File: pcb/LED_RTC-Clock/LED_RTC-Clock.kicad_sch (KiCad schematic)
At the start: 5 parts, among them J1 Jack_DC_5V, J2 LED_Matrix, J3 LED_DC, J4 RTC

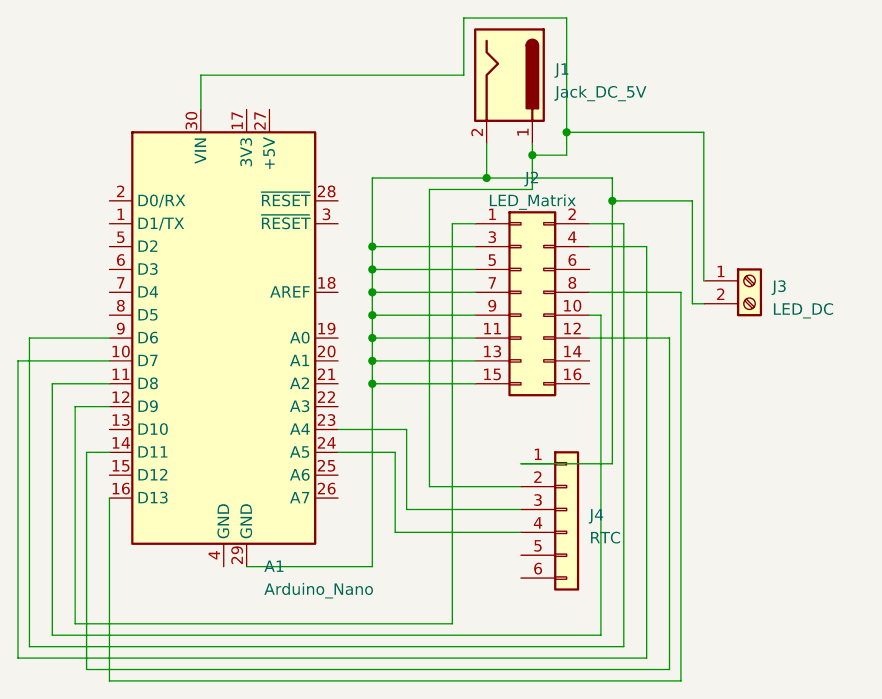
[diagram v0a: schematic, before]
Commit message: Updated PCB and Schematic
Updated the PCB and schematics to add a potentiometer for brightness control. Also tidied up traces, modified silkscreens and finalised board layout. Silkscreened V1.0
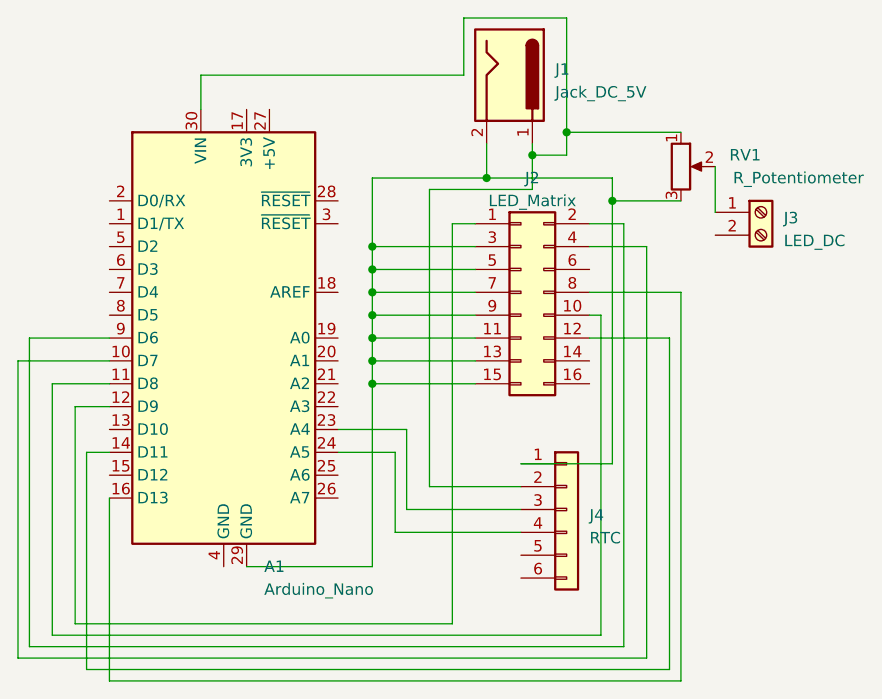
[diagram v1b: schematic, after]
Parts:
- added RV1: R_Potentiometer, Potentiometer_THT:Potentiometer_Alps_RK09L_Single_Horizontal, symbol Device:R_Potentiometer
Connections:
- net at A1.29 (GND), J1.2, J2.11 (C)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: now also RV1.3; no longer J3.2 (Pin_2)
- net at A1.30 (VIN), J1.1, J4.2 (VCC): now also RV1.1; no longer J3.1 (Pin_1)
- new net: J3.1 (Pin_1), RV1.2
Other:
- moved on the sheet: J3
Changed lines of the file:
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@@
 (kicad_sch (version 20230121) (generator eeschema)
   (paper "A4")
+  (junction (at 110.49 85.09) (diameter 0) (color 0 0 0 0)
+  )
+  (junction (at 97.79 95.25) (diameter 0) (color 0 0 0 0)
+  )
   (junction (at 124.46 87.63) (diameter 0) (color 0 0 0 0)
   )
-  (junction (at 110.49 85.09) (diameter 0) (color 0 0 0 0)
-  )
-  (junction (at 97.79 95.25) (diameter 0) (color 0 0 0 0)
-  )
   (junction (at 115.57 82.55) (diameter 0) (color 0 0 0 0)
   )
@@
     (stroke (width 0) (type default))
   )
+  (wire (pts (xy 135.89 83.82) (xy 135.89 88.9))
+    (stroke (width 0) (type default))
+  )
   (wire (pts (xy 104.14 119.38) (xy 114.3 119.38))
     (stroke (width 0) (type default))
@@
     (stroke (width 0) (type default))
   )
-  (wire (pts (xy 134.62 80.01) (xy 119.38 80.01))
+  (wire (pts (xy 132.08 80.01) (xy 119.38 80.01))
     (stroke (width 0) (type default))
   )
@@
     (stroke (width 0) (type default))
   )
+  (wire (pts (xy 124.46 87.63) (xy 132.08 87.63))
+    (stroke (width 0) (type default))
+  )
   (wire (pts (xy 97.79 102.87) (xy 109.22 102.87))
     (stroke (width 0) (type default))
@@
     (stroke (width 0) (type default))
   )
-  (wire (pts (xy 134.62 96.52) (xy 134.62 80.01))
-    (stroke (width 0) (type default))
-  )
   (wire (pts (xy 115.57 86.36) (xy 104.14 86.36))
     (stroke (width 0) (type default))
@@
     (stroke (width 0) (type default))
   )
+  (wire (pts (xy 124.46 85.09) (xy 124.46 87.63))
+    (stroke (width 0) (type default))
+  )
+  (wire (pts (xy 107.95 73.66) (xy 107.95 67.31))
+    (stroke (width 0) (type default))
+  )
+  (wire (pts (xy 64.77 134.62) (xy 64.77 110.49))
+    (stroke (width 0) (type default))
+  )
+  (wire (pts (xy 58.42 138.43) (xy 58.42 105.41))
+    (stroke (width 0) (type default))
+  )
+  (wire (pts (xy 119.38 67.31) (xy 119.38 80.01))
+    (stroke (width 0) (type default))
+  )
+  (wire (pts (xy 121.92 102.87) (xy 130.81 102.87))
+    (stroke (width 0) (type default))
+  )
+  (wire (pts (xy 104.14 86.36) (xy 104.14 119.38))
+    (stroke (width 0) (type default))
+  )
+  (wire (pts (xy 110.49 85.09) (xy 124.46 85.09))
+    (stroke (width 0) (type default))
+  )
   (wire (pts (xy 124.46 87.63) (xy 124.46 116.84))
     (stroke (width 0) (type default))
   )
-  (wire (pts (xy 133.35 87.63) (xy 124.46 87.63))
-    (stroke (width 0) (type default))
-  )
-  (wire (pts (xy 107.95 73.66) (xy 107.95 67.31))
-    (stroke (width 0) (type default))
-  )
-  (wire (pts (xy 64.77 134.62) (xy 64.77 110.49))
-    (stroke (width 0) (type default))
-  )
-  (wire (pts (xy 58.42 138.43) (xy 58.42 105.41))
-    (stroke (width 0) (type default))
-  )
-  (wire (pts (xy 119.38 67.31) (xy 119.38 80.01))
-    (stroke (width 0) (type default))
-  )
-  (wire (pts (xy 121.92 102.87) (xy 130.81 102.87))
-    (stroke (width 0) (type default))
-  )
-  (wire (pts (xy 104.14 86.36) (xy 104.14 119.38))
-    (stroke (width 0) (type default))
-  )
-  (wire (pts (xy 110.49 85.09) (xy 124.46 85.09))
-    (stroke (width 0) (type default))
-  )
   (wire (pts (xy 107.95 67.31) (xy 119.38 67.31))
     (stroke (width 0) (type default))
   )
-  (wire (pts (xy 124.46 85.09) (xy 124.46 87.63))
-    (stroke (width 0) (type default))
-  )
   (wire (pts (xy 97.79 97.79) (xy 97.79 95.25))
     (stroke (width 0) (type default))
@@
     (stroke (width 0) (type default))
   )
-  (wire (pts (xy 133.35 99.06) (xy 133.35 87.63))
-    (stroke (width 0) (type default))
-  )
   (wire (pts (xy 130.81 102.87) (xy 130.81 139.7))
     (stroke (width 0) (type default))
@@
     (stroke (width 0) (type default))
   )
-  (wire (pts (xy 134.62 99.06) (xy 133.35 99.06))
-    (stroke (width 0) (type default))
+  (symbol (lib_id "Device:R_Potentiometer") (at 132.08 83.82 0) (unit 1)
+    (in_bom yes) (on_board yes) (dnp no)
+    (property "Reference" "RV1" (at 140.97 82.55 0)
+      (effects (font (size 1.27 1.27)) (justify right))
+    )
+    (property "Value" "R_Potentiometer" (at 152.4 85.09 0)
+      (effects (font (size 1.27 1.27)) (justify right))
+    )
+    (property "Footprint" "Potentiometer_THT:Potentiometer_Alps_RK09L_Single_Horizontal" (at 132.08 83.82 0)
+      (effects (font (size 1.27 1.27)) hide)
+    )
+    (property "Datasheet" "~" (at 132.08 83.82 0)
+      (effects (font (size 1.27 1.27)) hide)
+    )
+    (pin "1")
+    (pin "2")
+    (pin "3")
+    (instances
+      (project "LED_RTC-Clock"
+        (path "/08a4b0e9-a9cd-416a-a6ab-1049ee8d191f"
+          (reference "RV1") (unit 1)
+        )
+      )
+    )
   )
   (symbol (lib_id "MCU_Module:Arduino_Nano_v2.x") (at 81.28 102.87 0) (unit 1)
@@
     )
   )
-  (symbol (lib_id "Connector:Screw_Terminal_01x02") (at 139.7 96.52 0) (unit 1)
+  (symbol (lib_id "Connector:Screw_Terminal_01x02") (at 140.97 88.9 0) (unit 1)
     (in_bom yes) (on_board yes) (dnp no) (fields_autoplaced)
-    (property "Reference" "J3" (at 142.24 97.155 0)
-      (effects (font (size 1.27 1.27)) (justify left))
-    )
-    (property "Value" "LED_DC" (at 142.24 99.695 0)
-      (effects (font (size 1.27 1.27)) (justify left))
-    )
-    (property "Footprint" "TerminalBlock:TerminalBlock_bornier-2_P5.08mm" (at 139.7 96.52 0)
-      (effects (font (size 1.27 1.27)) hide)
-    )
-    (property "Datasheet" "~" (at 139.7 96.52 0)
-      (effects (font (size 1.27 1.27)) hide)
-    )
+    (property "Reference" "J3" (at 143.51 89.535 0)
+      (effects (font (size 1.27 1.27)) (justify left))
+    )
+    (property "Value" "LED_DC" (at 143.51 92.075 0)
+      (effects (font (size 1.27 1.27)) (justify left))
+    )
+    (property "Footprint" "TerminalBlock:TerminalBlock_bornier-2_P5.08mm" (at 140.97 88.9 0)
+      (effects (font (size 1.27 1.27)) hide)
+    )
+    (property "Datasheet" "~" (at 140.97 88.9 0)
+      (effects (font (size 1.27 1.27)) hide)
+    )
